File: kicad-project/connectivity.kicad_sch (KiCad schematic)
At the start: 8 parts

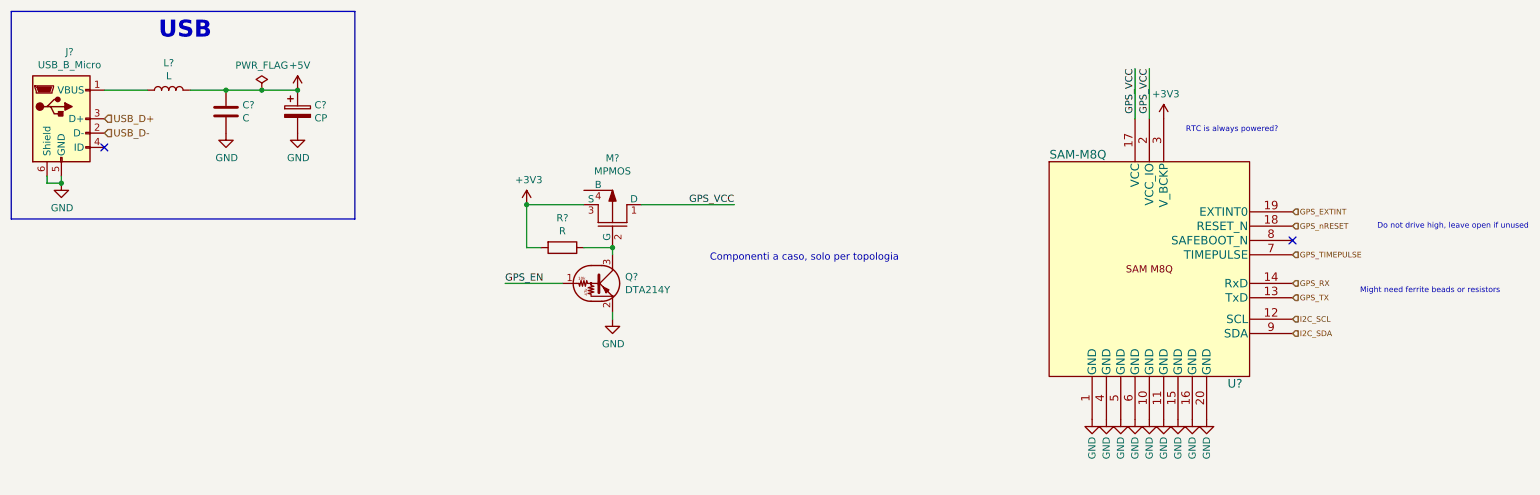
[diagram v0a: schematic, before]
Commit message: hw: add flash, switching circuit and XOUT resistor, change GPS and general cleanup
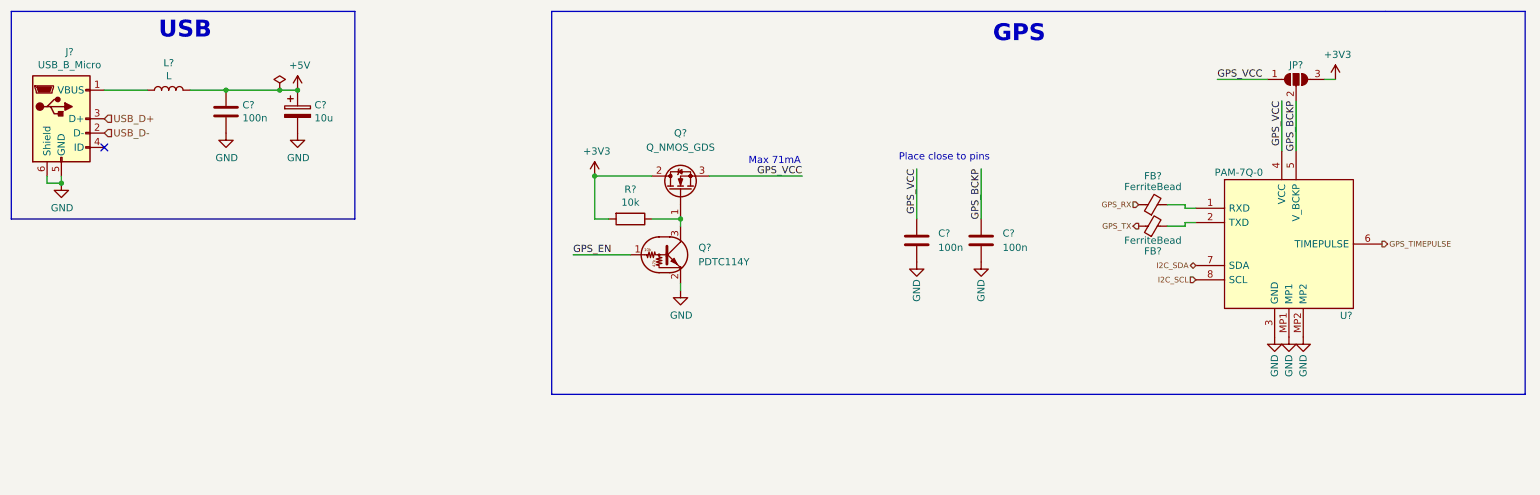
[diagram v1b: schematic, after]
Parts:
- removed M?: MPMOS, symbol pspice:MPMOS
- removed Q?: DTA214Y, symbol Transistor_BJT:DTA214Y
- removed U?: SAM-M8Q, AA_PPSE_2021:SAM-M8Q, symbol AA_PPSE_2021:SAM-M8Q
- added C? (x2): 100n, symbol Device:C
- added FB? (x2): FerriteBead, symbol Device:FerriteBead_Small
- added JP?: SolderJumper_3_Open, symbol Jumper:SolderJumper_3_Open
- added Q?: Q_NMOS_GDS, symbol Device:Q_NMOS_GDS
- added Q?: PDTC114Y, symbol Transistor_BJT:DTC114Y
- added U?: PAM-7Q-0, PAM7Q0, symbol PPSE_2021:PAM-7Q-0
- C?: value C -> 100n
- C?: value CP -> 10u
- R?: value R -> 10k
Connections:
- net +3V3: now also JP?.3 (B), Q?.2 (D)
- net GND: now also C?.2, C?.2, Q?.2 (E), U?.3 (GND), U?.MP1, U?.MP2
- net GPS_EN: now also Q?.1 (B)
- net GPS_RX: now also FB?.1
- net GPS_TIMEPULSE: now also U?.6 (TIMEPULSE)
- net GPS_TX: now also FB?.1
- net GPS_VCC: now also C?.1, JP?.1 (A), Q?.3 (S), U?.4 (VCC)
- net I2C_SCL: now also U?.8 (SCL)
- net I2C_SDA: now also U?.7 (SDA)
- net at R?.1: now also Q?.1 (G), Q?.3 (C)
- new net: FB?.2, U?.1 (RXD)
- new net: FB?.2, U?.2 (TXD)
- new net GPS_BCKP: C?.1, JP?.2 (C), U?.5 (V_BCKP)
- no-connect marks 2 -> 1
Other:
- note added: "GPS"
- note added: "Max 71mA"
- note added: "Place close to pins"
- note removed: "Componenti a caso, solo per topologia"
- note removed: "Do not drive high, leave open if unused"
- note removed: "Might need ferrite beads or resistors"
- note removed: "RTC is always powered?"
- company: (none) -> Connectivity
- moved on the sheet: R?

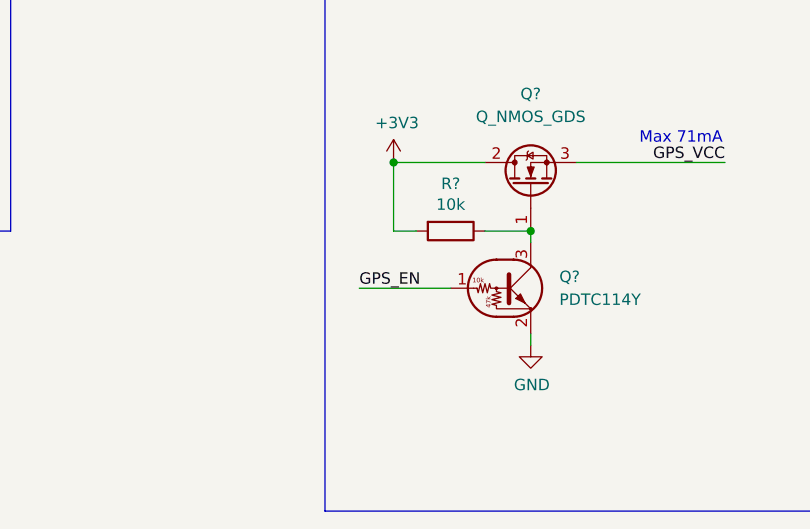
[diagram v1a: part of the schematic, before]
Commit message: hw: add panel sensing and change GPS_EN to hierarchical pin
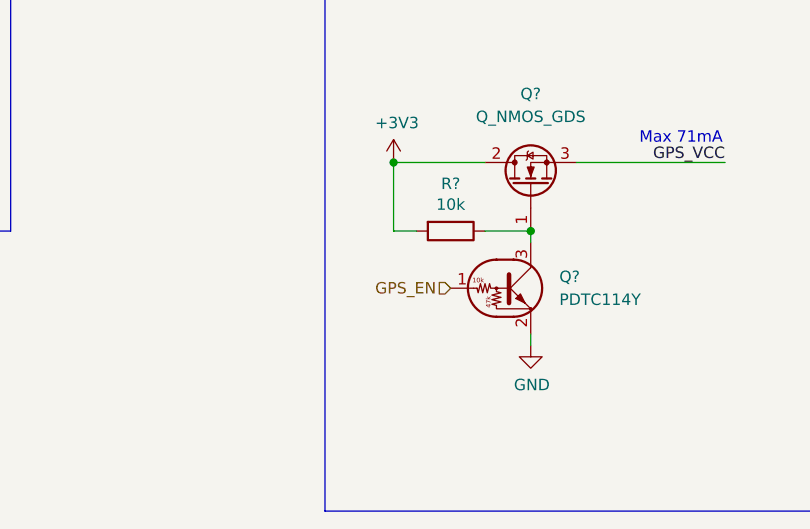
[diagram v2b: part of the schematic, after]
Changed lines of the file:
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@@
-    (stroke (width 0) (type default) (color 0 0 0 0))
-  )
-  (wire (pts (xy 113.665 57.15) (xy 123.825 57.15))
     (stroke (width 0) (type default) (color 0 0 0 0))
   )
@@
   )
   (text "Place close to pins" (at 171.45 40.64 0)
-    (effects (font (size 1.27 1.27)) (justify left bottom))
-  )
-  (label "GPS_EN" (at 113.665 57.15 0)
     (effects (font (size 1.27 1.27)) (justify left bottom))
   )
@@
     (effects (font (size 0.9906 0.9906)) (justify right))
   )
+  (hierarchical_label "GPS_EN" (shape input) (at 123.825 57.15 180)
+    (effects (font (size 1.27 1.27)) (justify right))
+  )
   (symbol (lib_id "Device:R") (at 123.825 50.8 270) (unit 1)

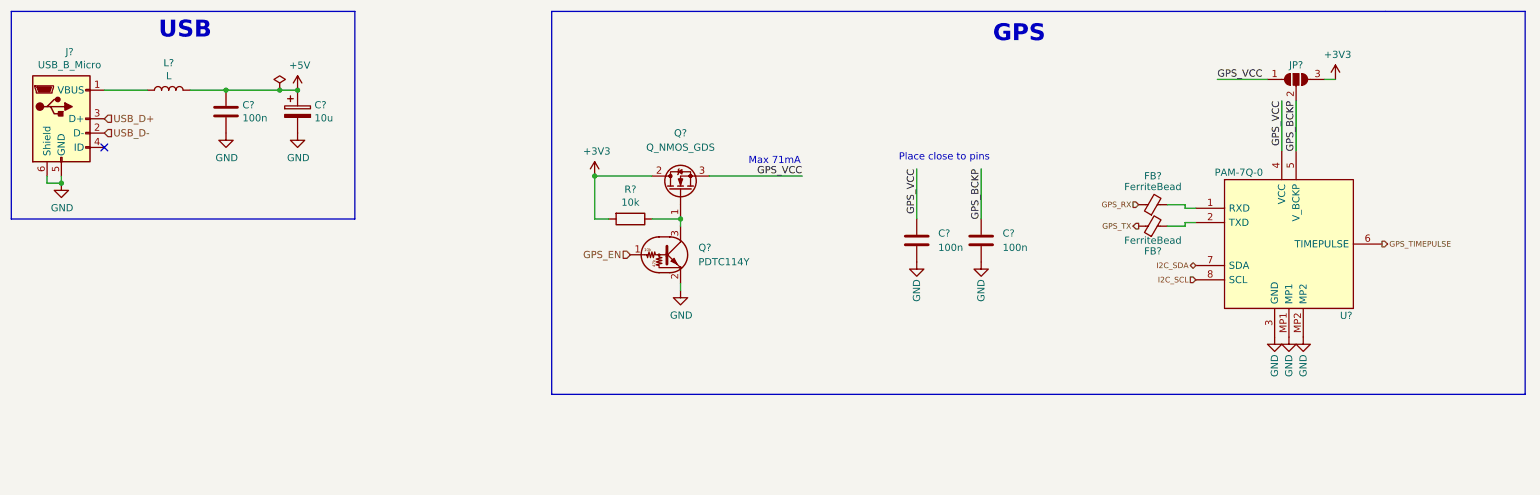
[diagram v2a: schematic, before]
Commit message: hw: add limit switches, dual power input, actuation sheet, debug and expansion connectors and connect sheets
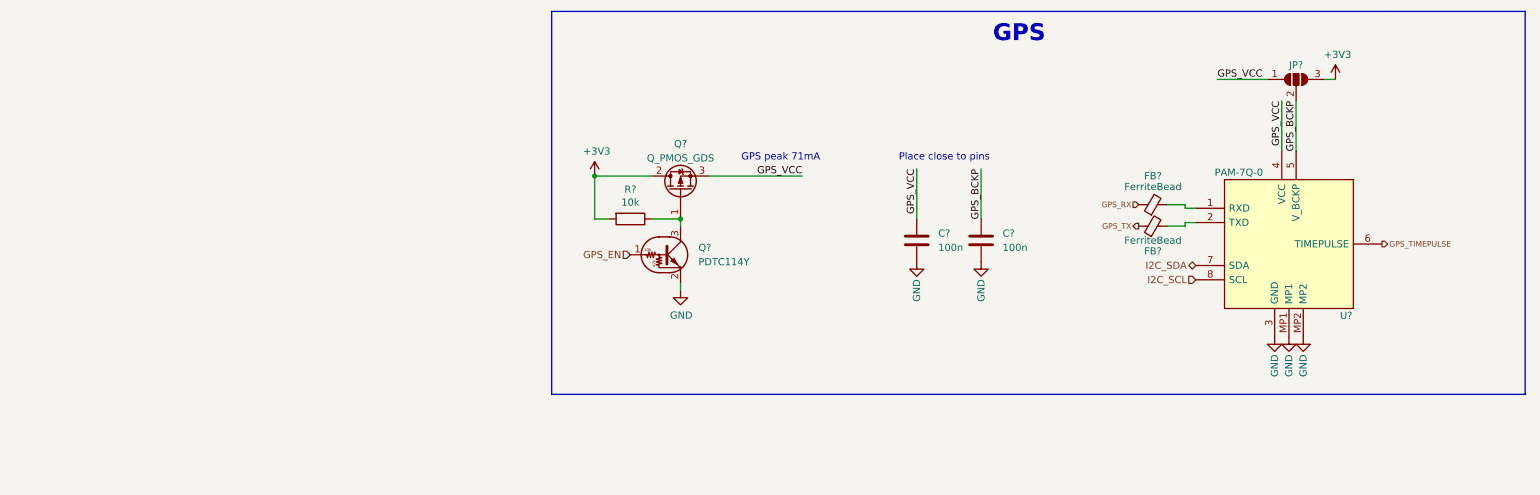
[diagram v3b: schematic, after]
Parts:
- removed C?: 100n, symbol Device:C
- removed C?: 10u, symbol Device:CP
- removed J?: USB_B_Micro, symbol Connector:USB_B_Micro
- removed L?: L, symbol Device:L
- removed Q?: Q_NMOS_GDS, symbol Device:Q_NMOS_GDS
- added Q?: Q_PMOS_GDS, symbol Device:Q_PMOS_GDS
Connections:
- net +3V3: now also Q?.2 (D)
- net GPS_VCC: now also Q?.3 (S)
- net at Q?.3 (C), R?.1: now also Q?.1 (G)
- no-connect marks 1 -> 0
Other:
- note added: "GPS peak 71mA"
- note removed: "Max 71mA"
- note removed: "USB"

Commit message: hw: schematic updates
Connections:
- net GND: no longer U?.MP1, U?.MP2
- net GPS_RX: now also U?.1 (RXD); no longer FB?.1
- net GPS_TX: now also U?.2 (TXD); no longer FB?.1
- net at FB?.2: no longer U?.1 (RXD)
- net at FB?.2: no longer U?.2 (TXD)
- no-connect marks 0 -> 2
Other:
- note added: "GPS Backup non serve."
- note added: "Make a check on i2c line of gps"
- note added: "Why UART e I2C?"
- note added: "not so clear"
- moved on the sheet: C?, FB?, JP?, Q?, R?, U?

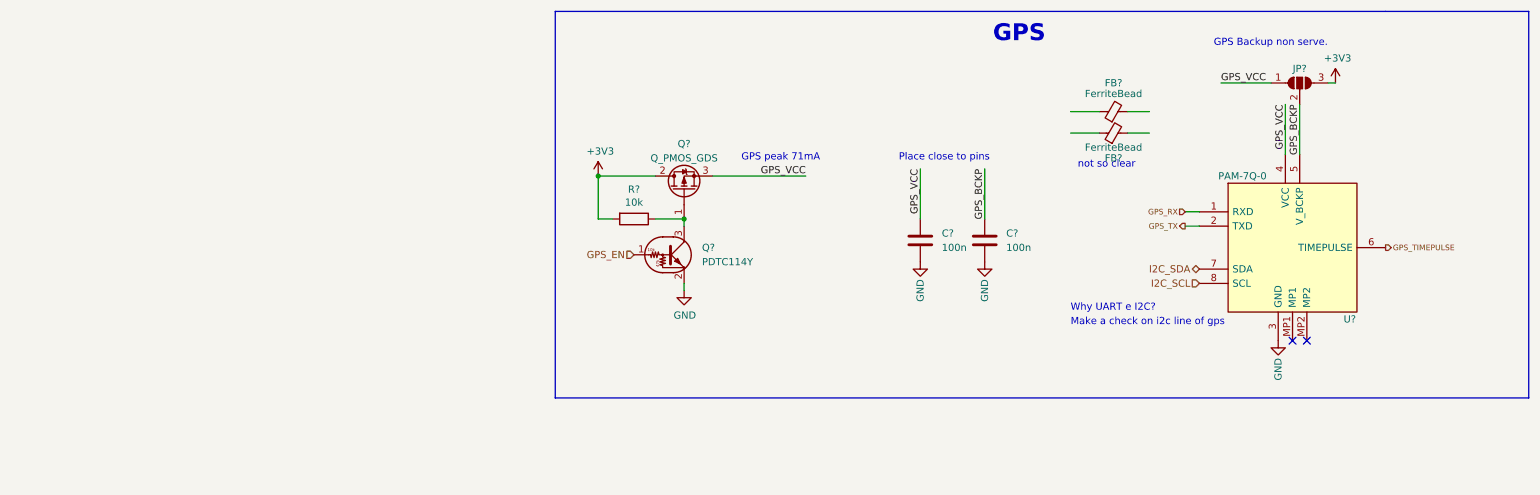
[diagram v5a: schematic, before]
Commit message: hw: update schematic pt. 2
add switching enable resistor, change usb inductor to ferrite bead, add OR gate and microstepping solder jumpers to motor driver, remove i2c and backup supply solder jumper from GPS, add ferrite bead to GPS, remove limit switches and other small changes
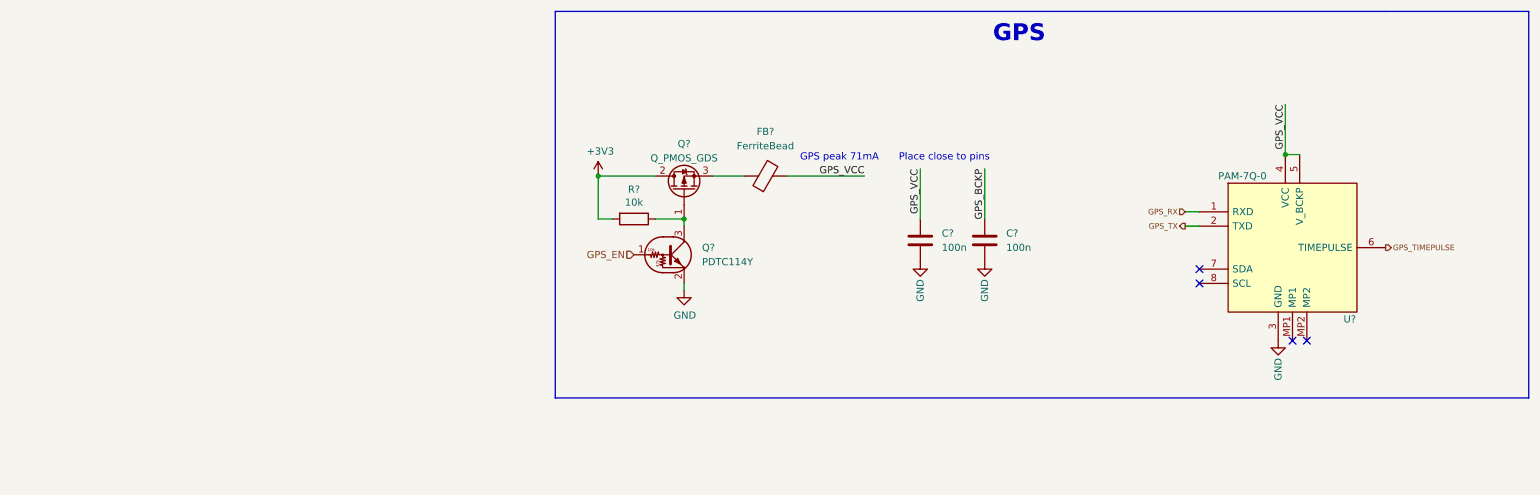
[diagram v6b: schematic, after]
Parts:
- removed FB? (x2): FerriteBead, symbol Device:FerriteBead_Small
- removed JP?: SolderJumper_3_Open, symbol Jumper:SolderJumper_3_Open
- added FB?: FerriteBead, symbol Device:FerriteBead
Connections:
- net GPS_BCKP: no longer U?.5 (V_BCKP)
- net GPS_VCC: now also U?.5 (V_BCKP), FB?.2; no longer Q?.3 (S)
- net I2C_SCL: no longer names the net of U?.8 (SCL)
- net I2C_SDA: no longer names the net of U?.7 (SDA)
- new net: FB?.1, Q?.3 (S)
- no-connect marks 2 -> 4
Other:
- note removed: "GPS Backup non serve."
- note removed: "Make a check on i2c line of gps"
- note removed: "Why UART e I2C?"
- note removed: "not so clear"
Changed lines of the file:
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@@
     (company "Connectivity")
   )
+  (junction (at 240.03 39.37) (diameter 0) (color 0 0 0 0)
+  )
   (junction (at 118.11 43.18) (diameter 0) (color 0 0 0 0)
   )
   (junction (at 133.35 50.8) (diameter 0) (color 0 0 0 0)
   )
+  (no_connect (at 224.79 62.23))
+  (no_connect (at 224.79 59.69))
   (no_connect (at 243.84 72.39))
   (no_connect (at 241.3 72.39))
@@
     (stroke (width 0) (type default) (color 0 0 0 0))
   )
-  (wire (pts (xy 212.09 35.56) (xy 215.9 35.56))
-    (stroke (width 0) (type default) (color 0 0 0 0))
-  )
   (wire (pts (xy 118.11 43.18) (xy 128.27 43.18))
     (stroke (width 0) (type default) (color 0 0 0 0))
@@
     (stroke (width 0) (type default) (color 0 0 0 0))
   )
-  (wire (pts (xy 247.65 26.67) (xy 248.92 26.67))
-    (stroke (width 0) (type default) (color 0 0 0 0))
-  )
   (wire (pts (xy 128.27 50.8) (xy 133.35 50.8))
     (stroke (width 0) (type default) (color 0 0 0 0))
@@
     (stroke (width 0) (type default) (color 0 0 0 0))
   )
-  (wire (pts (xy 201.93 35.56) (xy 207.01 35.56))
-    (stroke (width 0) (type default) (color 0 0 0 0))
-  )
   (wire (pts (xy 240.03 39.37) (xy 240.03 30.48))
     (stroke (width 0) (type default) (color 0 0 0 0))
   )
-  (wire (pts (xy 138.43 43.18) (xy 154.94 43.18))
-    (stroke (width 0) (type default) (color 0 0 0 0))
-  )
-  (wire (pts (xy 215.9 31.75) (xy 212.09 31.75))
+  (wire (pts (xy 138.43 43.18) (xy 144.018 43.18))
+    (stroke (width 0) (type default) (color 0 0 0 0))
+  )
+  (wire (pts (xy 151.638 43.18) (xy 165.354 43.18))
     (stroke (width 0) (type default) (color 0 0 0 0))
   )
@@
     (stroke (width 0) (type default) (color 0 0 0 0))
   )
-  (wire (pts (xy 242.57 30.48) (xy 242.57 39.37))
-    (stroke (width 0) (type default) (color 0 0 0 0))
-  )
   (wire (pts (xy 118.11 50.8) (xy 120.65 50.8))
     (stroke (width 0) (type default) (color 0 0 0 0))
   )
-  (wire (pts (xy 237.49 26.67) (xy 228.6 26.67))
-    (stroke (width 0) (type default) (color 0 0 0 0))
-  )
   (polyline (pts (xy 257.81 13.97) (xy 283.21 13.97))
     (stroke (width 0) (type default) (color 0 0 0 0))
@@
     (stroke (width 0) (type default) (color 0 0 0 0))
   )
-  (wire (pts (xy 201.93 31.75) (xy 207.01 31.75))
-    (stroke (width 0) (type default) (color 0 0 0 0))
-  )
   (wire (pts (xy 186.69 41.91) (xy 186.69 50.8))
     (stroke (width 0) (type default) (color 0 0 0 0))
@@
     (stroke (width 0) (type default) (color 0 0 0 0))
   )
-  (text "not so clear" (at 203.2 41.91 0)
-    (effects (font (size 1.27 1.27)) (justify left bottom))
-  )
-  (text "GPS peak 71mA" (at 143.51 40.64 0)
-    (effects (font (size 1.27 1.27)) (justify left bottom))
-  )
-  (text "Make a check on i2c line of gps\n" (at 201.93 69.85 0)
+  (wire (pts (xy 240.03 39.37) (xy 242.57 39.37))
+    (stroke (width 0) (type default) (color 0 0 0 0))
+  )
+  (text "GPS peak 71mA" (at 153.924 40.64 0)
     (effects (font (size 1.27 1.27)) (justify left bottom))
   )
@@
     (effects (font (size 1.27 1.27)) (justify left bottom))
   )
-  (text "GPS Backup non serve." (at 227.33 20.32 0)
-    (effects (font (size 1.27 1.27)) (justify left bottom))
-  )
-  (text "Why UART e I2C?" (at 201.93 67.31 0)
-    (effects (font (size 1.27 1.27)) (justify left bottom))
-  )
-  (label "GPS_VCC" (at 228.6 26.67 0)
-    (effects (font (size 1.27 1.27)) (justify left bottom))
-  )
   (label "GPS_VCC" (at 240.03 30.48 270)
     (effects (font (size 1.27 1.27)) (justify right bottom))
   )
-  (label "GPS_VCC" (at 154.94 43.18 180)
+  (label "GPS_VCC" (at 165.354 43.18 180)
     (effects (font (size 1.27 1.27)) (justify right bottom))
   )
@@
     (effects (font (size 1.27 1.27)) (justify right bottom))
   )
-  (label "GPS_BCKP" (at 242.57 30.48 270)
-    (effects (font (size 1.27 1.27)) (justify right bottom))
-  )
   (hierarchical_label "GPS_TX" (shape output) (at 222.25 52.07 180)
     (effects (font (size 0.9906 0.9906)) (justify right))
   )
-  (hierarchical_label "I2C_SCL" (shape input) (at 224.79 62.23 180)
-    (effects (font (size 1.27 1.27)) (justify right))
-  )
   (hierarchical_label "GPS_RX" (shape input) (at 222.25 49.53 180)
     (effects (font (size 0.9906 0.9906)) (justify right))
@@
   (hierarchical_label "GPS_TIMEPULSE" (shape output) (at 257.81 55.88 0)
     (effects (font (size 0.9906 0.9906)) (justify left))
-  )
-  (hierarchical_label "I2C_SDA" (shape bidirectional) (at 224.79 59.69 180)
-    (effects (font (size 1.27 1.27)) (justify right))
   )
   (hierarchical_label "GPS_EN" (shape input) (at 124.46 57.15 180)
@@
     (pin "1")
   )
-  (symbol (lib_id "power:+3V3") (at 248.92 26.67 0) (unit 1)
-    (in_bom yes) (on_board yes)
-    (property "Reference" "#PWR0157" (id 0) (at 248.92 30.48 0)
-      (effects (font (size 1.27 1.27)) hide)
-    )
-    (property "Value" "+3V3" (id 1) (at 249.301 22.2758 0))
-    (property "Footprint" "" (id 2) (at 248.92 26.67 0)
-      (effects (font (size 1.27 1.27)) hide)
-    )
-    (property "Datasheet" "" (id 3) (at 248.92 26.67 0)
-      (effects (font (size 1.27 1.27)) hide)
-    )
-    (pin "1")
-  )
   (symbol (lib_id "power:GND") (at 175.26 58.42 0) (unit 1)
     (in_bom yes) (on_board yes)
@@
     (pin "1")
   )
-  (symbol (lib_id "Device:FerriteBead_Small") (at 209.55 31.75 90) (unit 1)
-    (in_bom yes) (on_board yes)
-    (property "Reference" "FB?" (id 0) (at 209.55 26.67 90))
-    (property "Value" "FerriteBead" (id 1) (at 209.55 28.575 90))
-    (property "Footprint" "" (id 2) (at 209.55 33.528 90)
-      (effects (font (size 1.27 1.27)) hide)
-    )
-    (property "Datasheet" "~" (id 3) (at 209.55 31.75 0)
+  (symbol (lib_id "Device:FerriteBead") (at 147.828 43.18 90) (unit 1)
+    (in_bom yes) (on_board yes) (fields_autoplaced)
+    (property "Reference" "FB?" (id 0) (at 147.7772 35.306 90))
+    (property "Value" "FerriteBead" (id 1) (at 147.7772 37.846 90))
+    (property "Footprint" "" (id 2) (at 147.828 44.958 90)
+      (effects (font (size 1.27 1.27)) hide)
+    )
+    (property "Datasheet" "~" (id 3) (at 147.828 43.18 0)
       (effects (font (size 1.27 1.27)) hide)
     )
@@
     (pin "3")
   )
-  (symbol (lib_id "Device:FerriteBead_Small") (at 209.55 35.56 90) (unit 1)
-    (in_bom yes) (on_board yes)
-    (property "Reference" "FB?" (id 0) (at 209.55 40.005 90))
-    (property "Value" "FerriteBead" (id 1) (at 209.55 38.1 90))
-    (property "Footprint" "" (id 2) (at 209.55 37.338 90)
-      (effects (font (size 1.27 1.27)) hide)
-    )
-    (property "Datasheet" "~" (id 3) (at 209.55 35.56 0)
-      (effects (font (size 1.27 1.27)) hide)
-    )
-    (pin "1")
-    (pin "2")
-  )
   (symbol (lib_id "Device:Q_PMOS_GDS") (at 133.35 45.72 90) (unit 1)
     (in_bom yes) (on_board yes)
@@
       (effects (font (size 1.27 1.27)) hide)
     )
-    (pin "1")
-    (pin "2")
-    (pin "3")
-  )
-  (symbol (lib_id "Jumper:SolderJumper_3_Open") (at 242.57 26.67 0) (unit 1)
-    (in_bom yes) (on_board yes)
-    (property "Reference" "JP?" (id 0) (at 242.57 24.13 0))
-    (property "Value" "SolderJumper_3_Open" (id 1) (at 242.57 23.495 0)
-      (effects (font (size 1.27 1.27)) hide)
-    )
-    (property "Footprint" "" (id 2) (at 242.57 26.67 0)
-      (effects (font (size 1.27 1.27)) hide)
-    )
-    (property "Datasheet" "~" (id 3) (at 242.57 26.67 0)
-      (effects (font (size 1.27 1.27)) hide)
-    )
